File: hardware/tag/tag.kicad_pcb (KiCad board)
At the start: 2 copper layers, 50 x 52 mm, 119 parts, among them J1 USB_C_Receptacle_USB2.0_16P, J10 Conn_01x02, J2 BATTERY, J3 BLE_Conn, J4 SOURCE, J5 STM SWD, J6 I2C, J7 UART, J8 BLE SWD, J9 I2C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

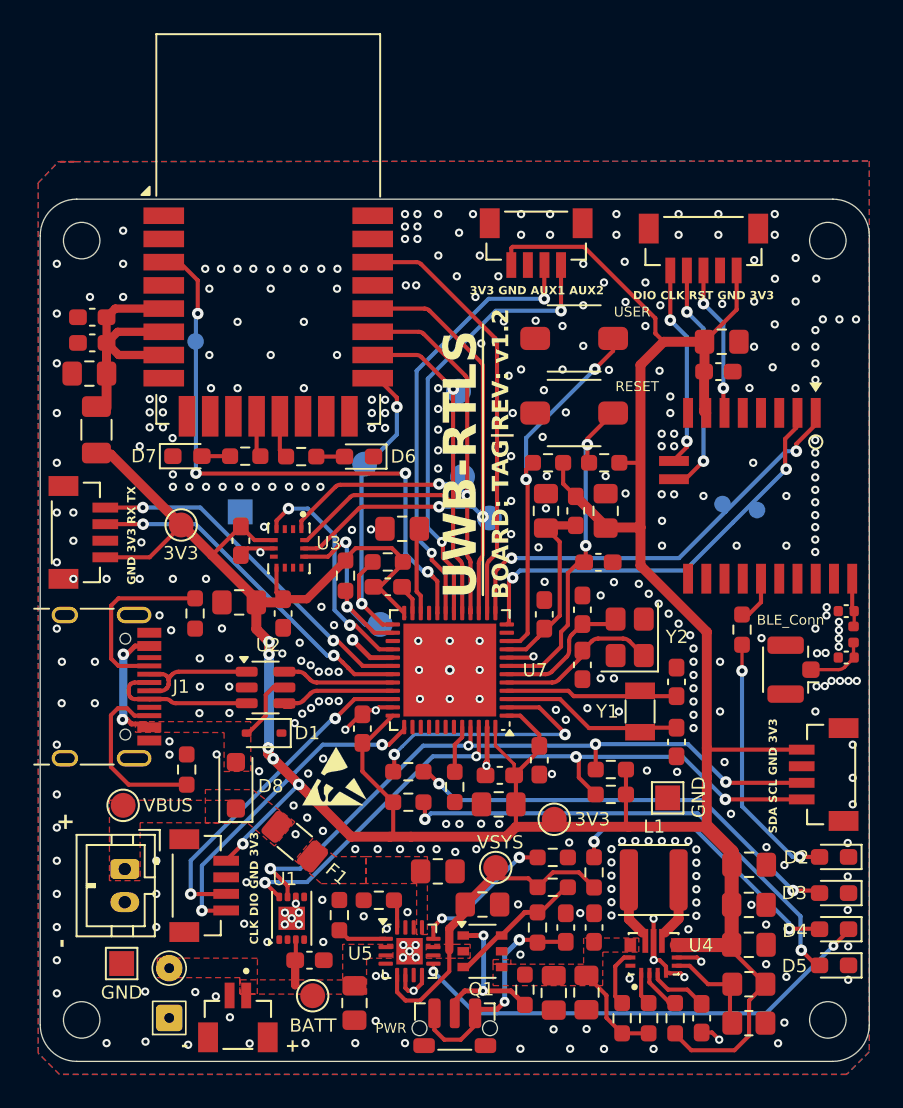
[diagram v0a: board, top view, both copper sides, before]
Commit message: Update: Change the on/off power logic on tag
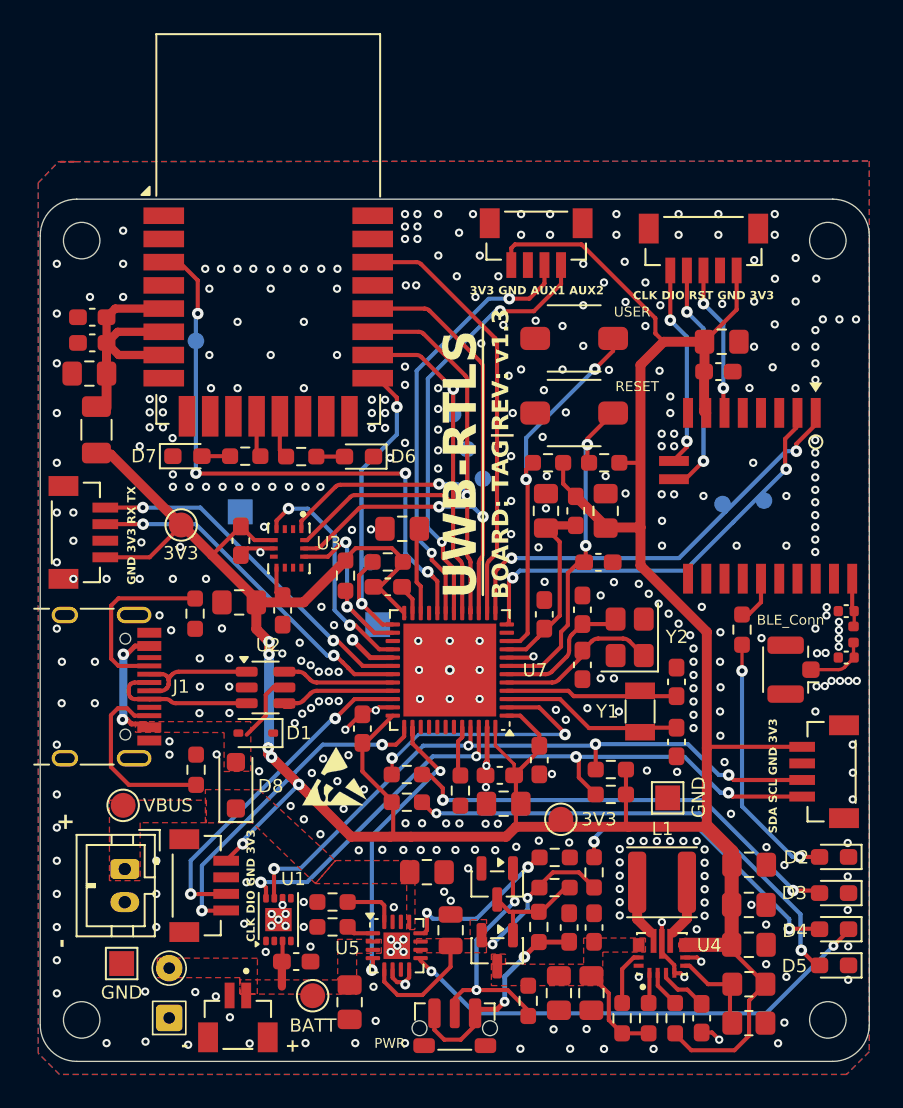
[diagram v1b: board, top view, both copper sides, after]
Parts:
- removed F1: Polyfuse_Small, Fuse:Fuse_1206_3216Metric
- removed Q1: AO664, Package_SO:TSOP-6_1.65x3.05mm_P0.95mm
- removed TP3: VSYS, TestPoint:TestPoint_Pad_D1.5mm
- added Q2: AO3400A, Package_TO_SOT_SMD:SOT-23, F.Cu at (58.6, 91.4)
- added Q3: AO3401A, Package_TO_SOT_SMD:SOT-23, F.Cu at (58.6, 95.4)
- C9: footprint Capacitor_SMD:C_0805_2012Metric_Pad1.18x1.45mm_HandSolder -> Capacitor_SMD:C_0805_2012Metric
- J9: value I2C -> AUX
- TP10, TP13, TP14, TP9: footprint TestPoint:TestPoint_Pad_D1.5mm -> TestPoint:TestPoint_Pad_D1.0mm
- moved TP14 5.92 mm to (50.9, 72.0)
- moved R6 2.79 mm to (48.6, 92.5)
- moved C9 2.47 mm to (55.8, 94.2), turned to 90 degrees
- moved TP9 2.40 mm to (57.7, 67.0)
- moved TP13 1.68 mm to (56.8, 65.2)
- moved TP10 1.43 mm to (55.9, 63.1)
- moved U5 0.84 mm to (52.5, 95.1)
- moved R8 0.82 mm to (48.6, 94.0), turned to 0 degrees
- moved C4 0.80 mm to (46.4, 96.1)
- moved U1 0.80 mm to (45.4, 93.5)
- moved TP11 0.71 mm to (74.7, 68.3)
- moved R14 0.70 mm to (60.4, 98.5)
- moved C6 0.66 mm to (54.3, 90.7)
- moved R3 0.57 mm to (40.4, 84.5)
- moved L1 0.52 mm to (68.5, 91.3)
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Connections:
- C6 pad 2: /VBUS_PROTECT -> VBUS
- U5 pad 13: /VBUS_PROTECT -> VBUS
- U5 pad 4: GND -> /CHARGE_EN
- U7 pad 38: /LED_PM -> /CHARGE_EN
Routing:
- net /CHARGE_EN: track 0.00 -> 18.5 mm, vias 0 -> 2
- net Net-(Q2-G): track 10.3 -> 15.6 mm
- net /SPI_MISO: track 33.0 -> 35.9 mm
- net /SPI_SCK: track 35.1 -> 37.4 mm
- net /SYS: track 19.5 -> 17.2 mm, vias 0 -> 2
- net Net-(Q2-D): track 8.30 -> 6.68 mm
- net GND: track 24.0 -> 22.4 mm, vias 381 -> 396
- net /SPI_MOSI: track 29.9 -> 31.4 mm
- net Net-(U5-TS): track 3.01 -> 1.68 mm
- net Net-(U5-ISET): track 2.20 -> 3.29 mm
- net /PB0 / ADC_IN8: track 27.3 -> 26.3 mm
- net Net-(U7-BOOT0): track 2.89 -> 3.69 mm
- net Net-(U5-ILIM): track 8.89 -> 9.67 mm
- net /CHG: track 29.2 -> 29.9 mm
- net Net-(D3-A): track 26.9 -> 27.6 mm
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- removed copper zone on F.Cu, net /VBUS_PROTECT
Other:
- board text added: "BOARD: TAG|REV: v1.3"
- board text added: "CLK DIO RST GND 3V3"
- board text added: "PRODUCTION BOARD REL: 2025-04-13"
- board text removed: "BOARD: TAG|REV: v1.2"
- board text removed: "DIO CLK RST GND 3V3"
- board text removed: "PRODUCTION BOARD REL: 2025-02-25"

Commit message: wip
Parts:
- moved D5 0.86 mm to (78.8, 95.5)
- moved D2 0.58 mm to (78.8, 90.3)
- moved D4 0.39 mm to (78.8, 93.8)
- moved D3 0.12 mm to (78.8, 92.0)
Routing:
- net Net-(D3-A): track 27.6 -> 28.3 mm
- net GND: vias 396 -> 395

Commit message: feat: Release final hardware for tag & anchor
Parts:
- C7: value 1u -> 100n
- Q2: value AO3400A -> AO3404A
- Q3: value AO3401A -> AO3407A
- R12: value 47K -> 100k
- R13: value 2.2k -> 10k
- R14: value 470K -> 10k
- TP10: value TestPoint -> MOSI
- TP11: value TestPoint -> TX
- TP12: value TestPoint -> RST
- TP13: value TestPoint -> MISO
- TP14: value TestPoint -> CS1
- TP15: value TestPoint -> CS2; footprint TestPoint:TestPoint_Pad_D1.5mm -> TestPoint:TestPoint_Pad_D1.0mm
- TP4: value TestPoint -> RX
- TP8: footprint TestPoint:TestPoint_Pad_D1.5mm -> TestPoint:TestPoint_Pad_1.0x1.0mm
- TP9: value TestPoint -> SCK
- moved TP8 20.0 mm to (62.5, 64.2)
- moved TP7 0.58 mm to (46.9, 98.2)
- moved C8 0.39 mm to (49.3, 98.5)
- moved R16 0.33 mm to (73.0, 76.1)
- moved TP15 0.10 mm to (51.4, 75.7)
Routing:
- net /LED_USR: track 16.3 -> 15.5 mm
- net GND: vias 395 -> 396
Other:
- board text added: "BOARD: TAG|REV: v1.4"
- board text removed: "BOARD: TAG|REV: v1.3"
- board text removed: "ID:"
